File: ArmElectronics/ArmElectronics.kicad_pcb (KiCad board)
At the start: 2 copper layers, 101 x 139 mm, 90 parts, among them J1 Raspberry_Pi_2_3, J10 AH1815 Breakout, J11 AH1815 Breakout, J12 AH1815 Breakout, J13 AH1815 Breakout, J14 AH1815 Breakout, J15 AH1815 Breakout, J16 AH1815 Breakout, J17 AH1815 Breakout, J18 AH1815 Breakout, J19 AH1815 Breakout, J2 Conn_01x14, J20 AH1815 Breakout, J21 1792245, J22 PA-09, J23 PA-09, J24 PA-09, J3 Encoder Breakout, J4 RasPi Power Out, J5 12V In, J6 Batt In, J7 Batt Out, J8 BNO055 QWIIC Conn, J9 AH1815 Breakout, U1 Teensy4.1, U12 74LVC1G97, U13 74LVC1G97, U14 74LVC1G97, U15 74LVC1G97, U16 74LVC1G97, U17 74LVC1G97, U2 Pololu_2857, U3 MAX11601, U4 Pololu_2851, U5 Pololu_3730, U6 TB9051FTG, U7 TB9051FTG, U8 TB9051FTG

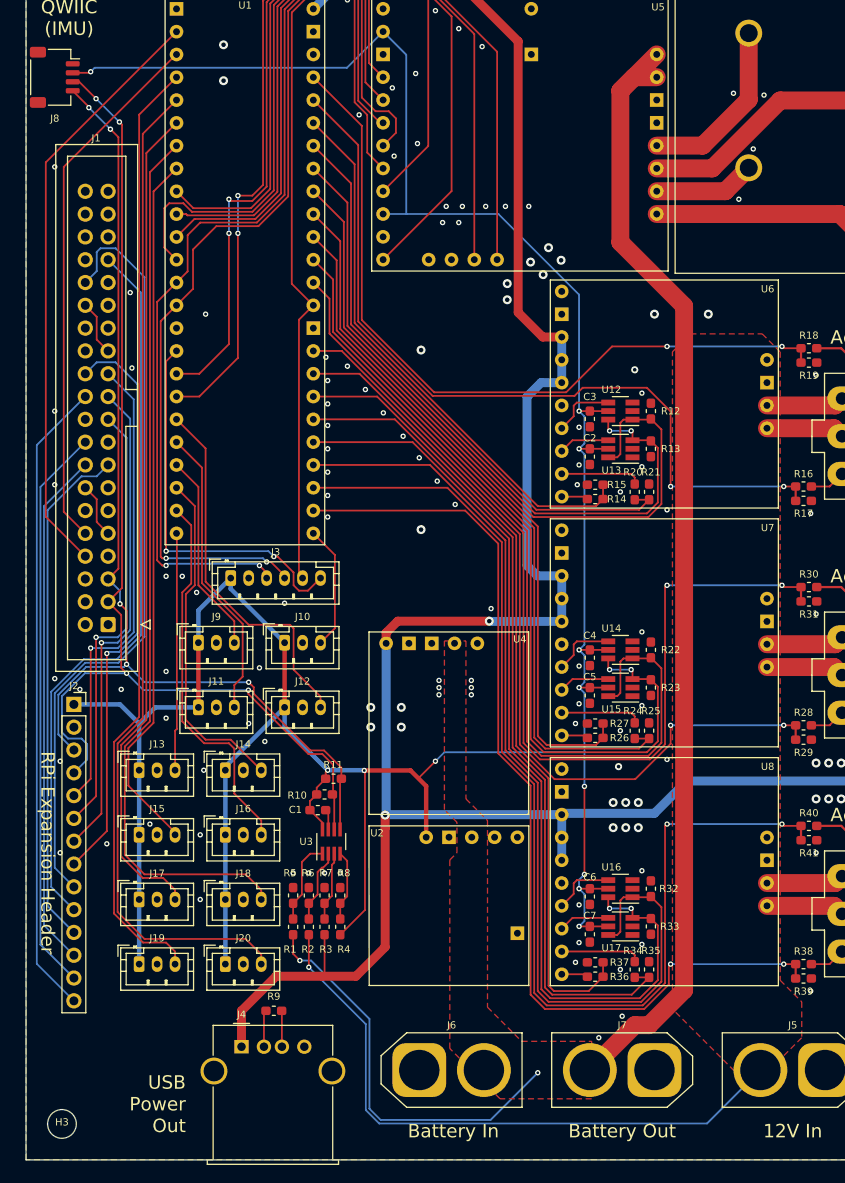
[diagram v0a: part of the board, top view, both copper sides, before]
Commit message: Added an E-Stop switch and motor off function
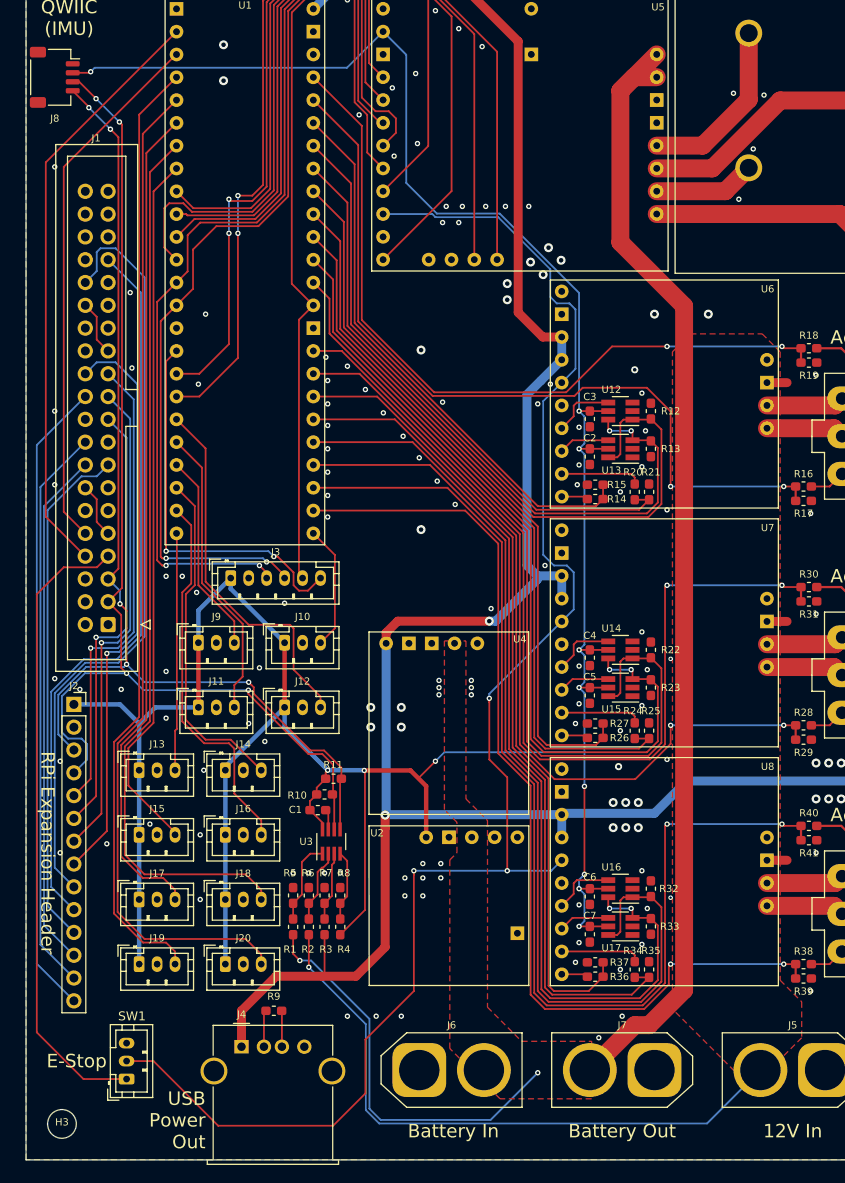
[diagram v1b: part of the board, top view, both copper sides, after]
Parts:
- added SW1: E-Stop, Connector_JST:JST_PH_B3B-PH-K_1x03_P2.00mm_Vertical, F.Cu at (193.2, 139.0)
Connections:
- J1 pad 7: Net-(J1-Pad7) -> /Motor_Enable
- U5 pad 10: +3V3 -> /~Disable
- U6 pad 5: +5V -> /~Disable
- U7 pad 5: +5V -> /~Disable
- U8 pad 5: +5V -> /~Disable
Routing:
- net /~Disable: track 0.00 -> 173.7 mm, vias 0 -> 3
- net /Motor_Enable: track 0.00 -> 70.7 mm
- net +5V: track 305.2 -> 298.4 mm
- net GND: track 14.5 -> 21.3 mm, vias 130 -> 150
- net +3V3: track 356.4 -> 351.9 mm
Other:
- board text added: "E-Stop"

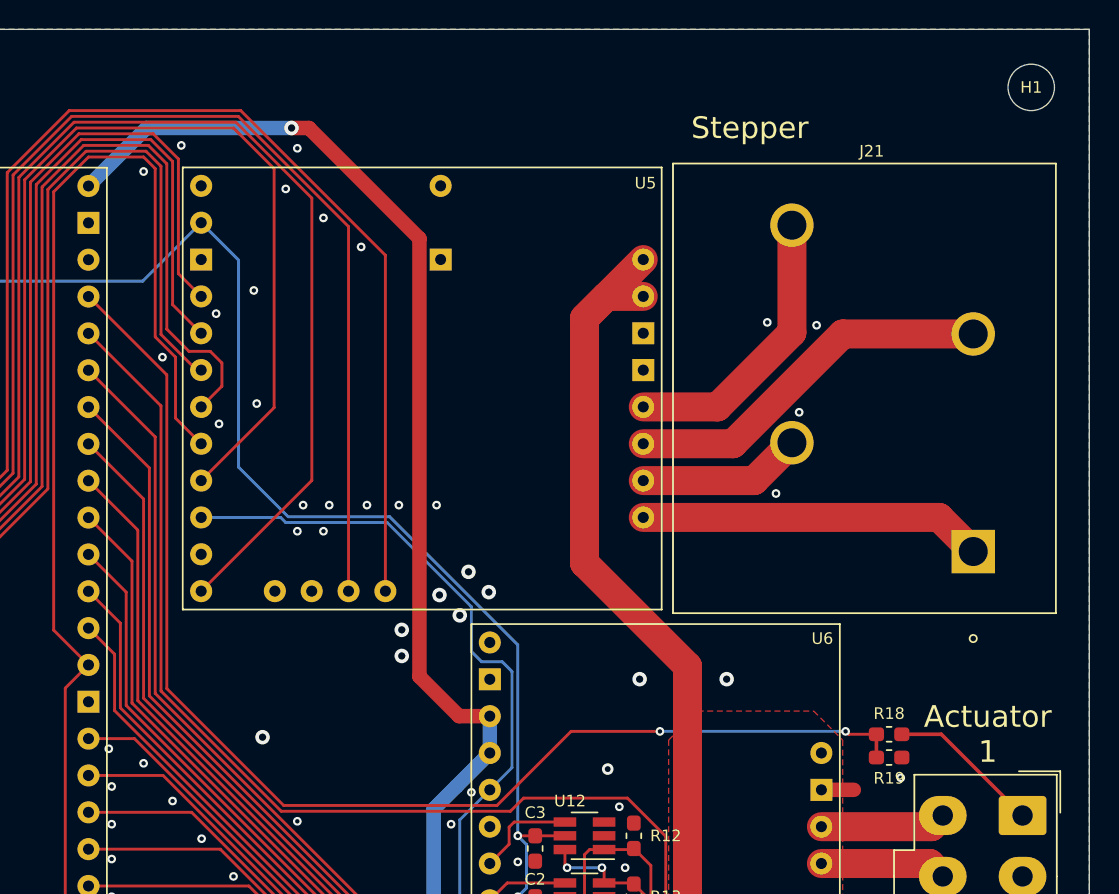
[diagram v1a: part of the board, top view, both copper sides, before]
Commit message: Added brake solenoid for axis 0
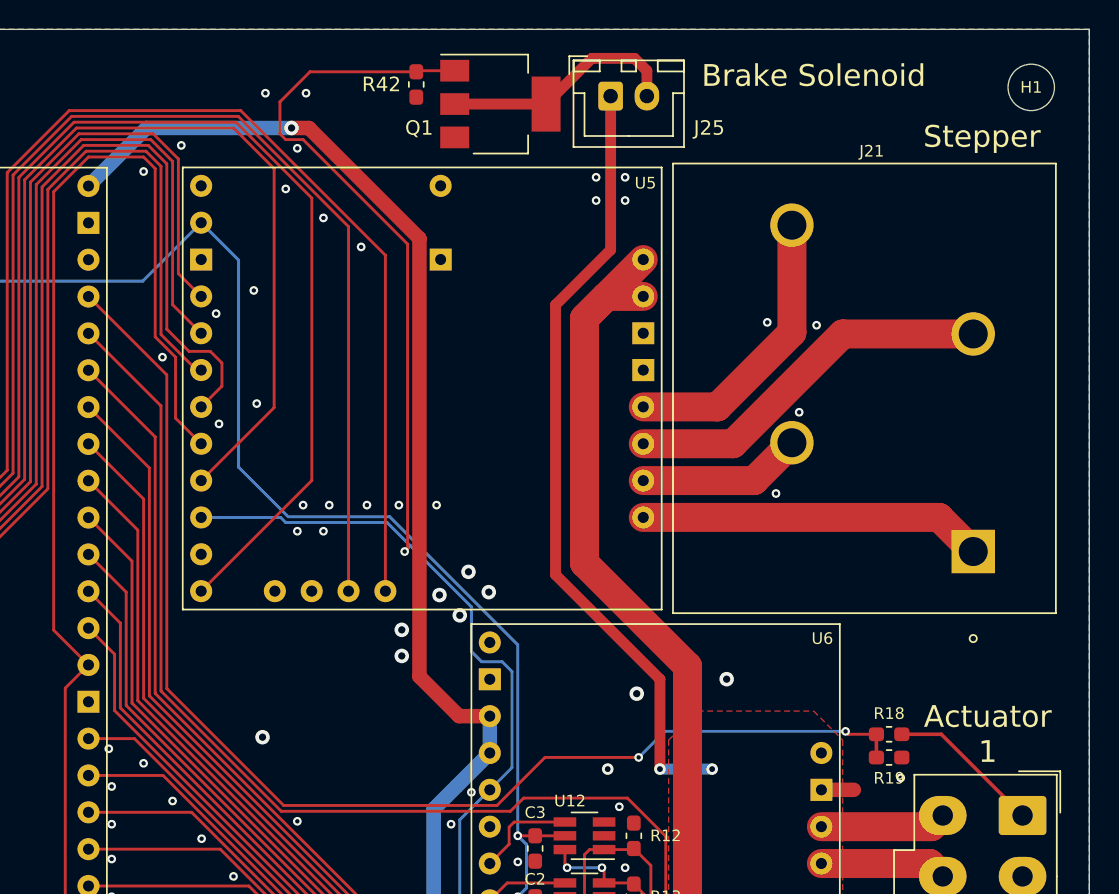
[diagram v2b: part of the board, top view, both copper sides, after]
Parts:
- added J25: Solenoid, Connector_JST:JST_XH_B2B-XH-A_1x02_P2.50mm_Vertical, F.Cu at (250.0, 13.6)
- added Q1: Q_NMOS_GDSD, Package_TO_SOT_SMD:SOT-223, F.Cu at (242.4, 14.2)
- added R42: 100k, Resistor_SMD:R_0603_1608Metric_Pad1.05x0.95mm_HandSolder, F.Cu at (236.6, 12.8)
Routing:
- net +12V: track 69.2 -> 123.8 mm, vias 1 -> 3
- net /~Disable: track 173.7 -> 222.6 mm, vias 3 -> 4
- net Net-(J25-Pad2): track 0.00 -> 16.7 mm
- net GND: vias 150 -> 156
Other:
- board text added: "Brake Solenoid"

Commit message: Forgot to fill a zone
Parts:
- J22, J23, J24: footprint Connector_Molex:Molex_Mini-Fit_Jr_5566-06A_2x03_P4.20mm_Vertical -> ArmElectronics_Footprints:Molex_Mini-Fit_Jr_5566-06A_2x03_P4.20mm_Vertical_3D

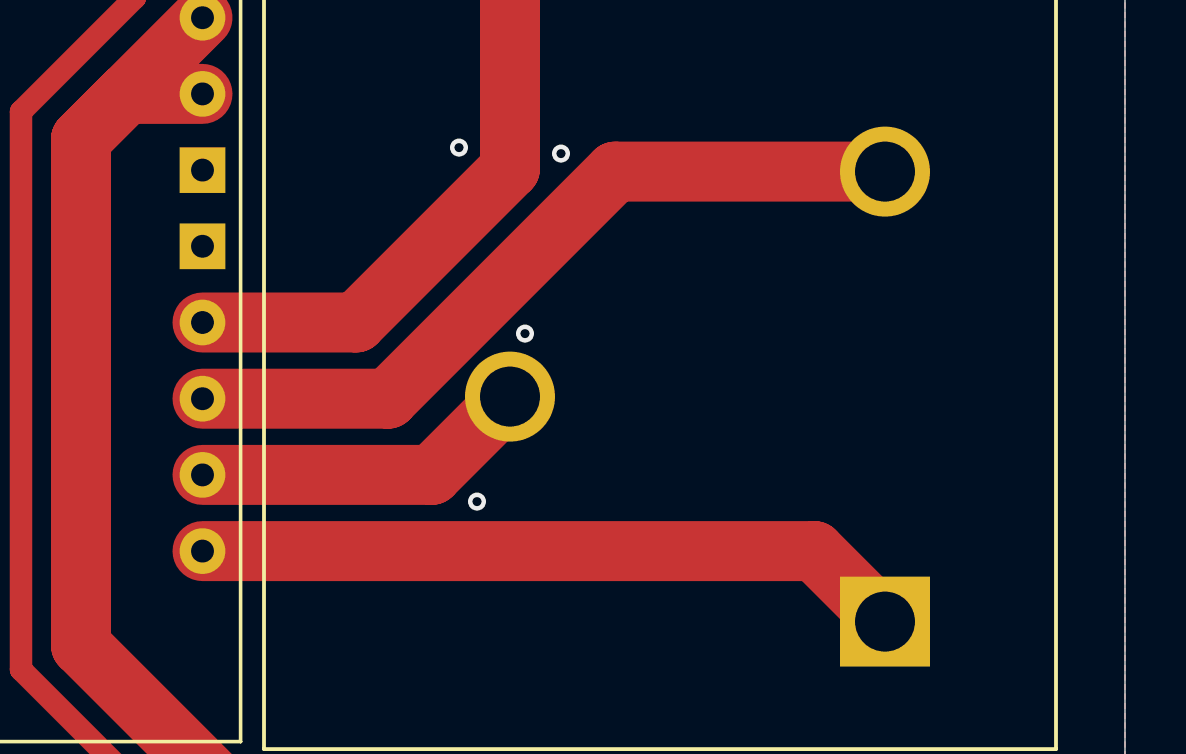
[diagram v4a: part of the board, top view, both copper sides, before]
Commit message: added an alternate stepper connector
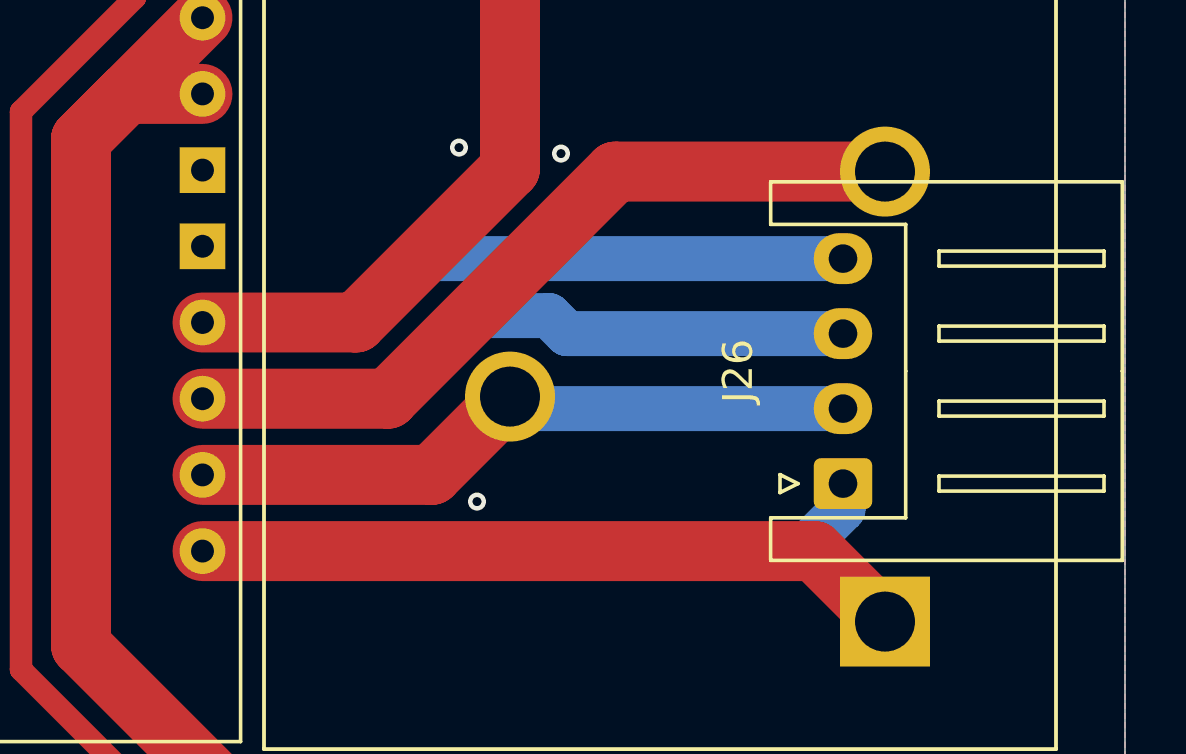
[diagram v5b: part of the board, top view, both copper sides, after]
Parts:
- added J26: Stepper Alternate Connection, Connector_JST:JST_XH_S4B-XH-A_1x04_P2.50mm_Horizontal, F.Cu at (273.6, 40.4)
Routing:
- net Net-(J21-Pad1): track 23.7 -> 46.5 mm
- net Net-(J21-Pad3): track 25.9 -> 48.6 mm
- net Net-(J21-Pad2): track 11.3 -> 33.6 mm
- net Net-(J21-Pad4): track 19.8 -> 42.0 mm
- net GND: vias 156 -> 155

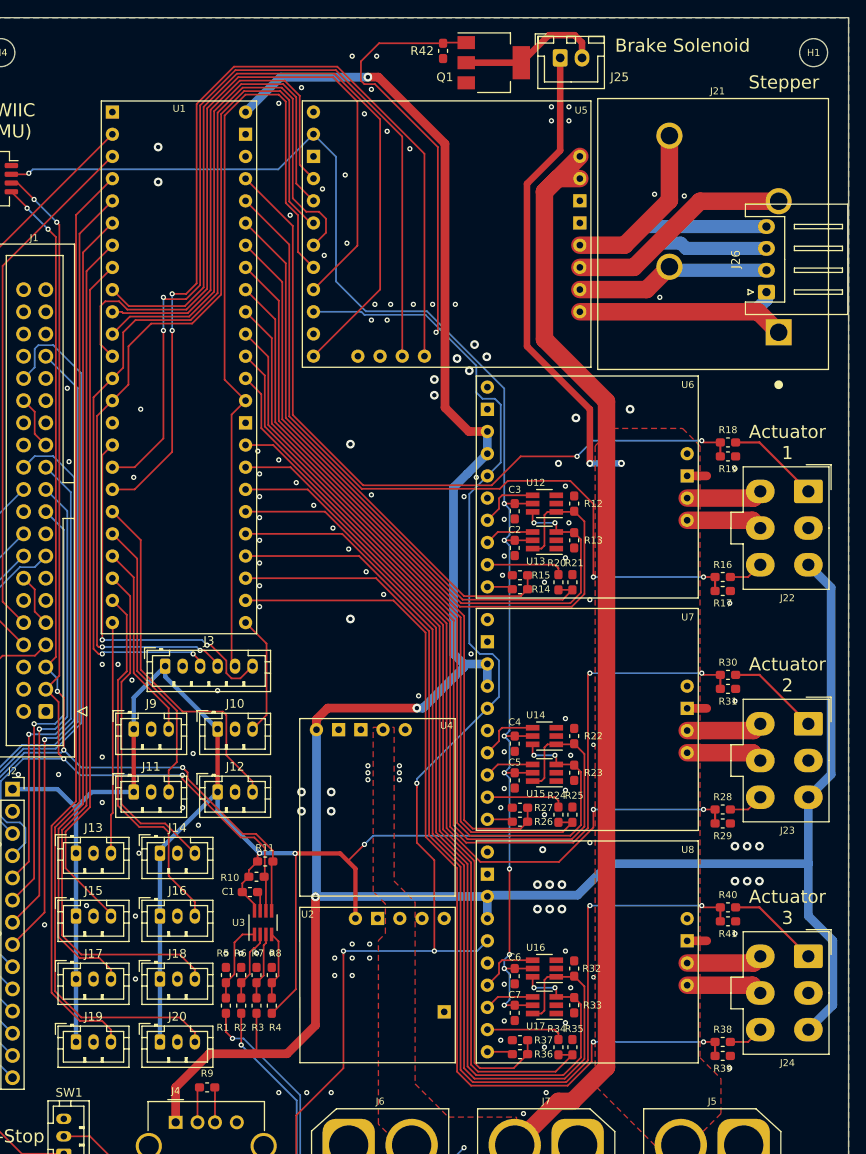
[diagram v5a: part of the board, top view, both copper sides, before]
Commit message: Added fan connectors
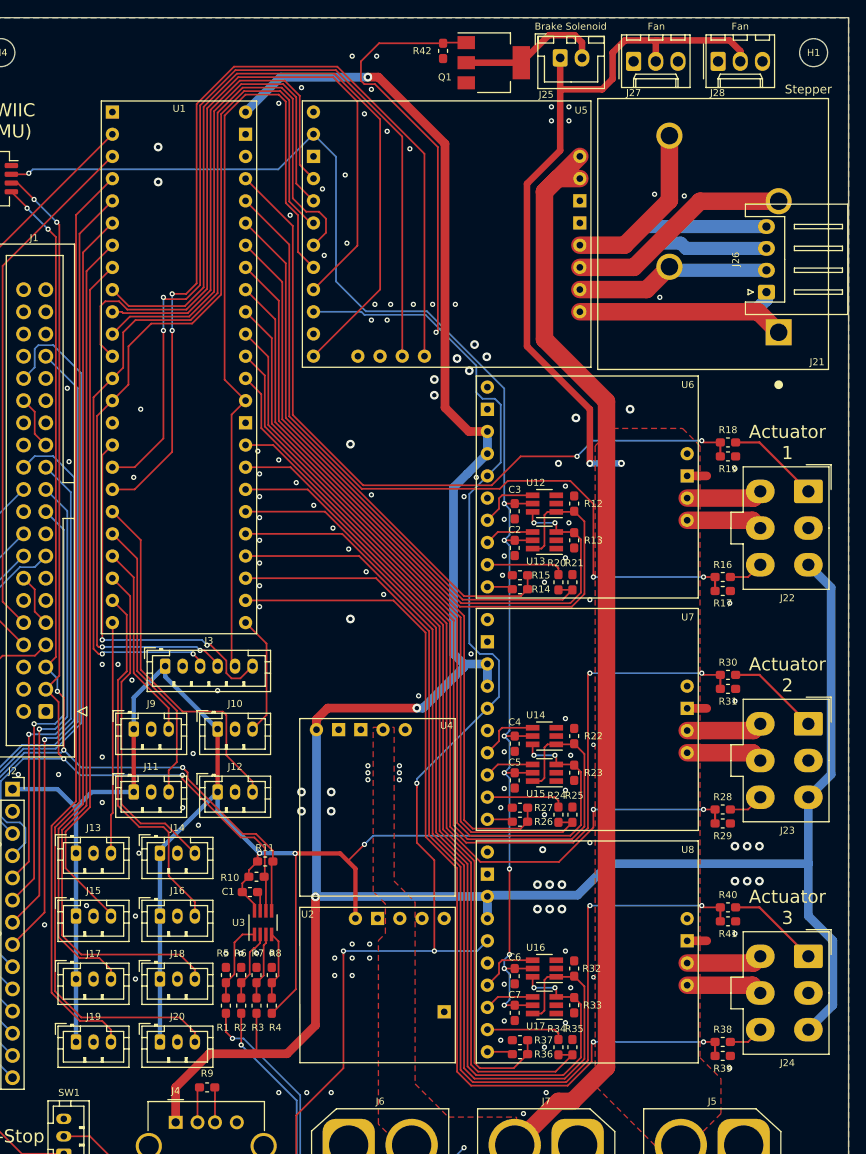
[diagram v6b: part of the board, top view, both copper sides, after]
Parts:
- added J27: Computer Fan, Connector_Molex:Molex_KK-254_AE-6410-03A_1x03_P2.54mm_Vertical, F.Cu at (258.4, 14.0)
- added J28: Computer Fan, Connector_Molex:Molex_KK-254_AE-6410-03A_1x03_P2.54mm_Vertical, F.Cu at (268.1, 14.0)
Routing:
- net +12V: track 123.8 -> 152.6 mm
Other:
- board text added: "Fan"

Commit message: Added fans
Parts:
- moved J26 161.2 mm to (113.6, 60.4)
- moved R16 161.2 mm to (108.6, 93.0)
- moved R17 161.2 mm to (108.6, 94.6)
- moved R28 161.2 mm to (108.6, 119.6)
- moved R29 161.2 mm to (108.6, 121.2)
- moved R38 161.2 mm to (108.6, 146.2)
- moved R39 161.2 mm to (108.6, 147.8)
- moved C1 161.2 mm to (54.5, 129.1)
- moved C2 161.2 mm to (84.8, 89.7)
- moved C3 161.2 mm to (84.8, 85.5)
- moved C4 161.2 mm to (84.8, 112.1)
- moved C5 161.2 mm to (84.8, 116.3)
- moved C6 161.2 mm to (84.8, 138.7)
- moved C7 161.2 mm to (84.8, 142.9)
- moved H1 161.2 mm to (119.0, 33.0)
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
